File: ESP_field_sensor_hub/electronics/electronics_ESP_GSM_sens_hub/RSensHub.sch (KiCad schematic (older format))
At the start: 42 parts, among them J1 RJ45_Shielded, J2 RJ45_Shielded, J4 Conn_01x04_Female, Q4 IRF540N, U1 MAX48_module, U10 PC817, U11 PC817, U12 PC817, U2 5V5ADCDC, U3 ESP32-WROOM-32U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

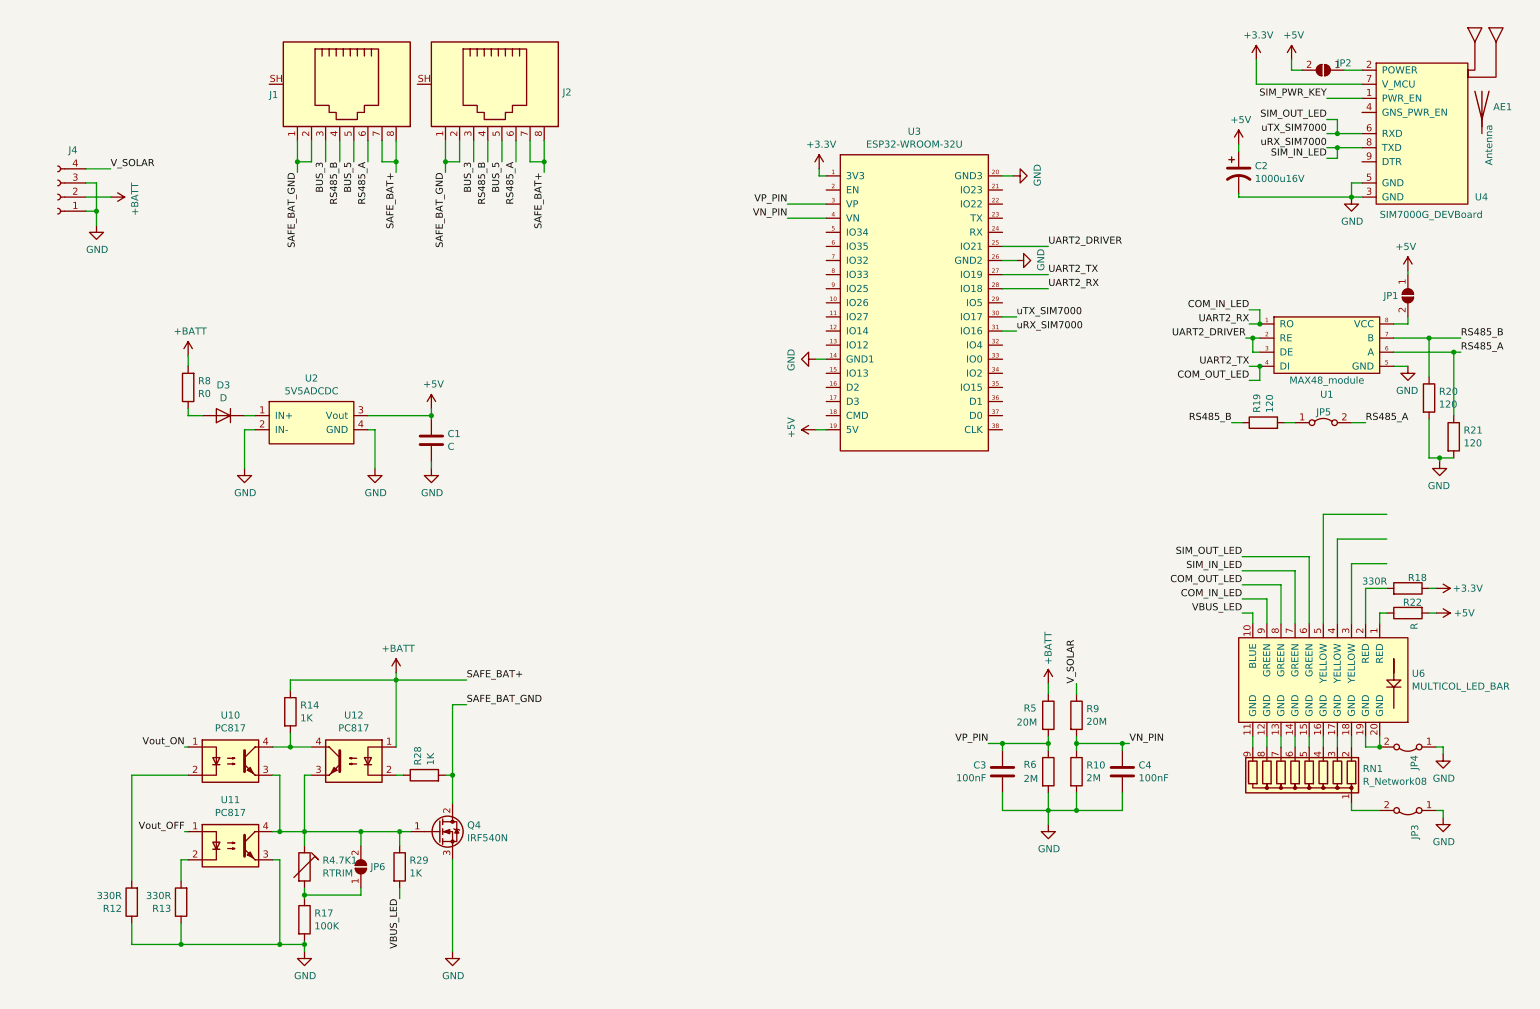
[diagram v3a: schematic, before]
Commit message: worked on sens hub PCB layout, mostly done, needs finishing touches
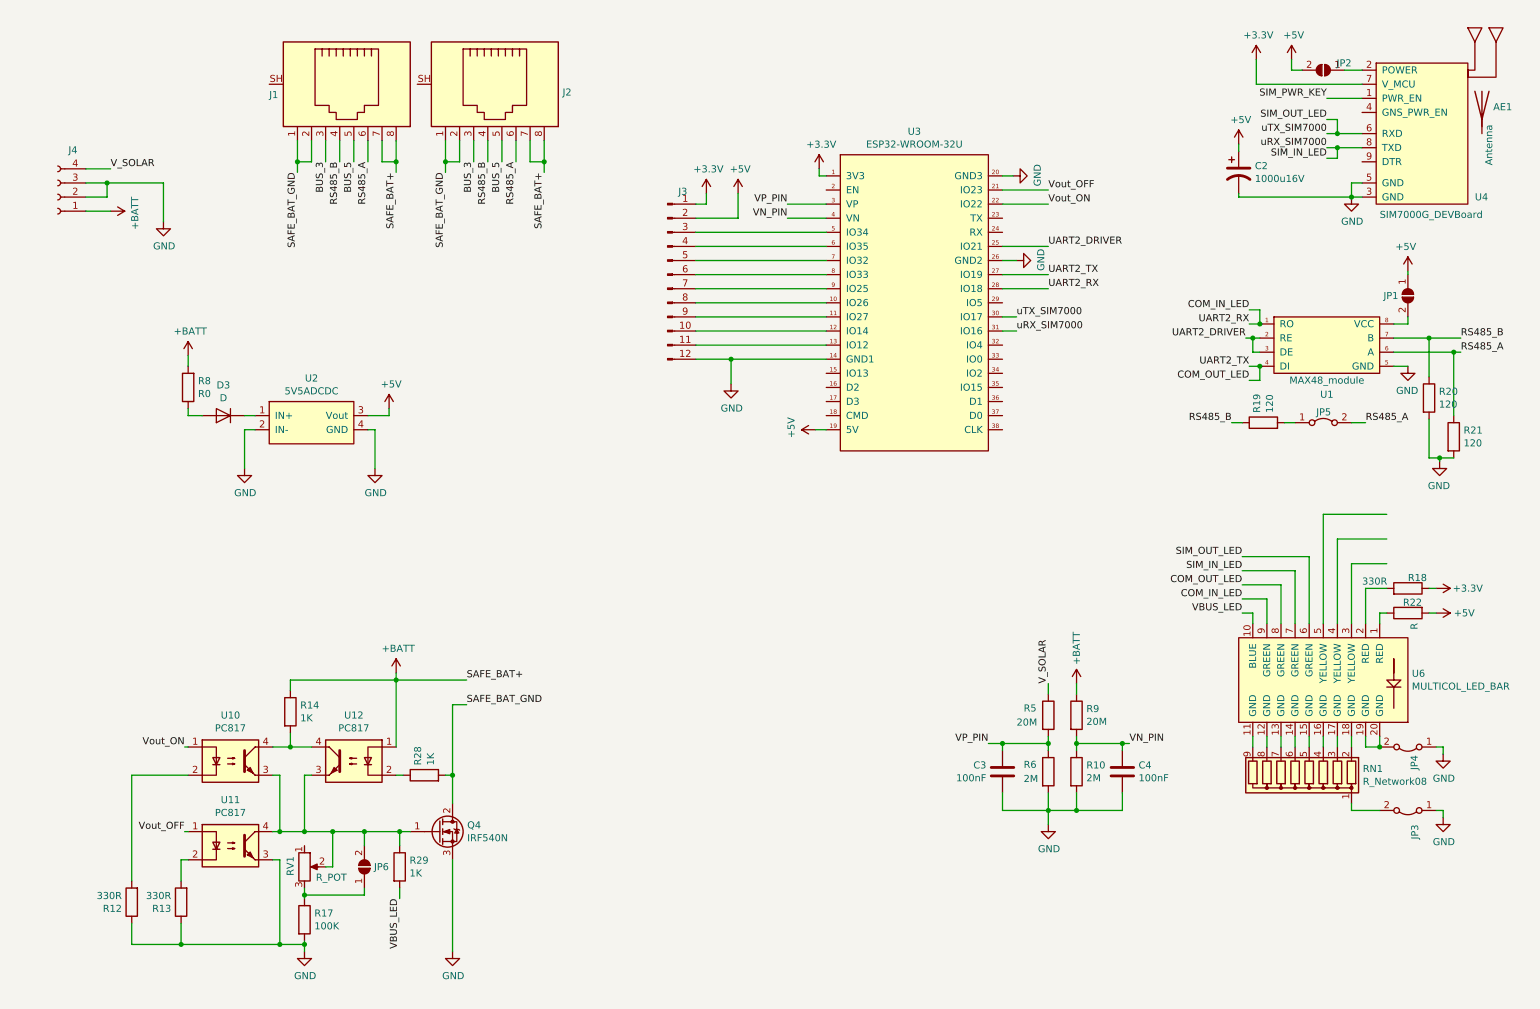
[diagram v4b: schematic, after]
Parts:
- removed C1: C, symbol Device:C
- removed R4.7K1: RTRIM, symbol Device:RTRIM
- added J3: Conn_01x12_Male, myComponents:PinHeader_1x12_P2.54mm_widePads, symbol Connector:Conn_01x12_Male
- added RV1: R_POT, myComponents:Potentiometer_ACP_CA9-V10_Vertical_Hole, symbol Device:R_POT
- D3: footprint (none) -> myComponents:1N41_Diode
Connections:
- net +3V3: now also J3.1 (Pin_1)
- net +5V: now also J3.2 (Pin_2)
- net +BATT: now also J4.1 (Pin_1), R9.1; no longer J4.2 (Pin_2), R5.1
- net GND: now also J4.2 (Pin_2), J3.12 (Pin_12); no longer J4.1 (Pin_1)
- net V_SOLAR: now also R5.1; no longer R9.1
- net Vout_OFF: now also U3.21 (IO23)
- net Vout_ON: now also U3.22 (IO22)
- net at U3.10 (IO26): now also J3.8 (Pin_8)
- net at U3.11 (IO27): now also J3.9 (Pin_9)
- net at U3.12 (IO14): now also J3.10 (Pin_10)
- net at U3.13 (IO12): now also J3.11 (Pin_11)
- net at U3.5 (IO34): now also J3.3 (Pin_3)
- net at U3.6 (IO35): now also J3.4 (Pin_4)
- net at U3.7 (IO32): now also J3.5 (Pin_5)
- net at U3.8 (IO33): now also J3.6 (Pin_6)
- net at U3.9 (IO25): now also J3.7 (Pin_7)
- net at JP6.2 (B), Q4.1 (G), R29.1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: now also RV1.2
- net at JP6.1 (A), R17.1: now also RV1.3
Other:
- moved on the sheet: JP6
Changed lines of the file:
@@
 L power:+BATT #PWR0111
 U 1 1 636D9491
-P 7825 5250
-F 0 "#PWR0111" H 7825 5100 50  0001 C CNN
-F 1 "+BATT" V 7825 5500 50  0000 C CNN
-F 2 "" H 7825 5250 50  0001 C CNN
-F 3 "" H 7825 5250 50  0001 C CNN
-	1    7825 5250
+P 8025 5250
+F 0 "#PWR0111" H 8025 5100 50  0001 C CNN
+F 1 "+BATT" V 8025 5500 50  0000 C CNN
+F 2 "" H 8025 5250 50  0001 C CNN
+F 3 "" H 8025 5250 50  0001 C CNN
+	1    8025 5250
 	1    0    0    -1
 $EndComp
@@
 	2200 3350 2125 3350
 Wire Wire Line
-	3000 3350 3450 3350
-Wire Wire Line
-	3450 3350 3450 3300
+	3150 3350 3150 3300
 $Comp
 L power:+5V #PWR0115
 U 1 1 636A3668
-P 3450 3300
-F 0 "#PWR0115" H 3450 3150 50  0001 C CNN
-F 1 "+5V" H 3465 3473 50  0000 C CNN
-F 2 "" H 3450 3300 50  0001 C CNN
-F 3 "" H 3450 3300 50  0001 C CNN
-	1    3450 3300
-	1    0    0    -1
-$EndComp
-$Comp
-L Device:C C1
-U 1 1 636A4A02
-P 3450 3525
-F 0 "C1" H 3565 3571 50  0000 L CNN
-F 1 "C" H 3565 3480 50  0000 L CNN
-F 2 "" H 3488 3375 50  0001 C CNN
-F 3 "~" H 3450 3525 50  0001 C CNN
-	1    3450 3525
-	1    0    0    -1
-$EndComp
-Wire Wire Line
-	3450 3375 3450 3350
-Connection ~ 3450 3350
-Wire Wire Line
-	3450 3675 3450 3725
-$Comp
-L power:GND #PWR0116
-U 1 1 636A7644
-P 3450 3725
-F 0 "#PWR0116" H 3450 3475 50  0001 C CNN
-F 1 "GND" H 3455 3552 50  0000 C CNN
-F 2 "" H 3450 3725 50  0001 C CNN
-F 3 "" H 3450 3725 50  0001 C CNN
-	1    3450 3725
+P 3150 3300
+F 0 "#PWR0115" H 3150 3150 50  0001 C CNN
+F 1 "+5V" H 3165 3473 50  0000 C CNN
+F 2 "" H 3150 3300 50  0001 C CNN
+F 3 "" H 3150 3300 50  0001 C CNN
+	1    3150 3300
 	1    0    0    -1
 $EndComp
@@
 F 0 "D3" H 1975 3134 50  0000 C CNN
 F 1 "D" H 1975 3225 50  0000 C CNN
-F 2 "" H 1975 3350 50  0001 C CNN
+F 2 "myComponents:1N41_Diode" H 1975 3350 50  0001 C CNN
 F 3 "~" H 1975 3350 50  0001 C CNN
 	1    1975 3350
@@
 Wire Wire Line
 	8025 5325 8025 5250
-Text Label 8025 5250 1    50   ~ 0
+Text Label 7825 5250 1    50   ~ 0
 V_SOLAR
 Wire Wire Line
@@
 	-1   0    0    1
 $EndComp
-$Comp
-L power:+BATT #PWR0130
-U 1 1 63985720
-P 1175 1800
-F 0 "#PWR0130" H 1175 1650 50  0001 C CNN
-F 1 "+BATT" H 1190 1973 50  0000 C CNN
-F 2 "" H 1175 1800 50  0001 C CNN
-F 3 "" H 1175 1800 50  0001 C CNN
-	1    1175 1800
-	0    1    1    0
-$EndComp
-$Comp
-L power:GND #PWR0131
-U 1 1 6398F99C
-P 1075 2000
-F 0 "#PWR0131" H 1075 1750 50  0001 C CNN
-F 1 "GND" H 1080 1827 50  0000 C CNN
-F 2 "" H 1075 2000 50  0001 C CNN
-F 3 "" H 1075 2000 50  0001 C CNN
-	1    1075 2000
-	1    0    0    -1
-$EndComp
-Wire Wire Line
-	1000 1900 1075 1900
-Wire Wire Line
-	1075 1900 1075 2000
-Wire Wire Line
-	1000 1700 1075 1700
-Wire Wire Line
-	1075 1700 1075 1900
-Connection ~ 1075 1900
 Text Label 1175 1600 0    50   ~ 0
 V_SOLAR
@@
 L power:GND #PWR0136
 U 1 1 63D67849
-P 6175 2950
-F 0 "#PWR0136" H 6175 2700 50  0001 C CNN
-F 1 "GND" H 6180 2777 50  0000 C CNN
-F 2 "" H 6175 2950 50  0001 C CNN
-F 3 "" H 6175 2950 50  0001 C CNN
-	1    6175 2950
-	0    1    1    0
-$EndComp
-Wire Wire Line
-	6175 2950 6250 2950
+P 5575 3125
+F 0 "#PWR0136" H 5575 2875 50  0001 C CNN
+F 1 "GND" H 5580 2952 50  0000 C CNN
+F 2 "" H 5575 3125 50  0001 C CNN
+F 3 "" H 5575 3125 50  0001 C CNN
+	1    5575 3125
+	1    0    0    -1
+$EndComp
 $Comp
 L power:+5V #PWR0137
@@
 Text Label 4250 1625 3    50   ~ 0
 SAFE_BAT+
-Wire Wire Line
-	1000 1800 1175 1800
 $Comp
 L Isolator:PC817 U12
@@
 Wire Wire Line
 	3250 5900 3200 5900
-$Comp
-L Device:RTRIM R4.7K1
-U 1 1 6425482E
-P 2550 6550
-F 0 "R4.7K1" H 2678 6596 50  0000 L CNN
-F 1 "RTRIM" H 2678 6505 50  0000 L CNN
-F 2 "" V 2480 6550 50  0001 C CNN
-F 3 "~" H 2550 6550 50  0001 C CNN
-	1    2550 6550
-	1    0    0    -1
-$EndComp
-Wire Wire Line
-	2550 6400 2550 6300
-Wire Wire Line
-	2550 6775 2550 6750
 Wire Wire Line
 	2550 7150 2550 7100
@@
 L Jumper:SolderJumper_2_Open JP6
 U 1 1 644467F2
-P 2950 6550
-F 0 "JP6" V 2950 6618 50  0000 L CNN
-F 1 "SolderJumper_2_Open" H 2950 6664 50  0001 C CNN
-F 2 "Jumper:SolderJumper-2_P1.3mm_Open_RoundedPad1.0x1.5mm" H 2950 6550 50  0001 C CNN
-F 3 "~" H 2950 6550 50  0001 C CNN
-	1    2950 6550
+P 2975 6550
+F 0 "JP6" V 2975 6618 50  0000 L CNN
+F 1 "SolderJumper_2_Open" H 2975 6664 50  0001 C CNN
+F 2 "Jumper:SolderJumper-2_P1.3mm_Open_RoundedPad1.0x1.5mm" H 2975 6550 50  0001 C CNN
+F 3 "~" H 2975 6550 50  0001 C CNN
+	1    2975 6550
 	0    1    -1   0
 $EndComp
 Wire Wire Line
-	2550 6300 2950 6300
-Wire Wire Line
-	2950 6750 2550 6750
-Wire Wire Line
-	2950 6700 2950 6750
-Connection ~ 2550 6750
-Wire Wire Line
-	2550 6750 2550 6700
-Wire Wire Line
-	2950 6400 2950 6300
-Connection ~ 2950 6300
-Wire Wire Line
-	2950 6300 3225 6300
+	2550 6300 2750 6300
 Connection ~ 3225 6300
 Wire Wire Line
@@
 Wire Wire Line
 	1700 5700 1725 5700
+$Comp
+L Device:R_POT RV1
+U 1 1 63DF64FA
+P 2550 6550
+F 0 "RV1" V 2450 6625 50  0000 R CNN
+F 1 "R_POT" H 2850 6475 50  0000 R CNN
+F 2 "myComponents:Potentiometer_ACP_CA9-V10_Vertical_Hole" H 2550 6550 50  0001 C CNN
+F 3 "~" H 2550 6550 50  0001 C CNN
+	1    2550 6550
+	1    0    0    -1
+$EndComp
+Wire Wire Line
+	2700 6550 2750 6550
+Wire Wire Line
+	2750 6550 2750 6300
+Connection ~ 2750 6300
+Wire Wire Line
+	2750 6300 2975 6300
+Wire Wire Line
+	2550 6700 2550 6750
+Wire Wire Line
+	2975 6400 2975 6300
+Connection ~ 2975 6300
+Wire Wire Line
+	2975 6300 3225 6300
+Wire Wire Line
+	2975 6700 2975 6750
+Wire Wire Line
+	2975 6750 2550 6750
+Connection ~ 2550 6750
+Wire Wire Line
+	2550 6750 2550 6775
+Text Label 7825 1850 0    50   ~ 0
+Vout_ON
+Text Label 7825 1750 0    50   ~ 0
+Vout_OFF
+Wire Wire Line
+	7500 1850 7825 1850
+Wire Wire Line
+	7825 1750 7500 1750
+Wire Wire Line
+	5325 2050 6250 2050
+Wire Wire Line
+	5325 2150 6250 2150
+Wire Wire Line
+	5325 2250 6250 2250
+Wire Wire Line
+	5325 2350 6250 2350
+Wire Wire Line
+	6250 2450 5325 2450
+Wire Wire Line
+	5325 2550 6250 2550
+Wire Wire Line
+	6250 2650 5325 2650
+Wire Wire Line
+	6250 2750 5325 2750
+Wire Wire Line
+	6250 2850 5325 2850
+$Comp
+L power:+3.3V #PWR0103
+U 1 1 63EBB881
+P 5400 1775
+F 0 "#PWR0103" H 5400 1625 50  0001 C CNN
+F 1 "+3.3V" H 5415 1948 50  0000 C CNN
+F 2 "" H 5400 1775 50  0001 C CNN
+F 3 "" H 5400 1775 50  0001 C CNN
+	1    5400 1775
+	1    0    0    -1
+$EndComp
+Wire Wire Line
+	5325 1850 5400 1850
+Wire Wire Line
+	5400 1850 5400 1775
+$Comp
+L power:+5V #PWR0104
+U 1 1 63ECC4A0
+P 5625 1775
+F 0 "#PWR0104" H 5625 1625 50  0001 C CNN
+F 1 "+5V" H 5640 1948 50  0000 C CNN
+F 2 "" H 5625 1775 50  0001 C CNN
+F 3 "" H 5625 1775 50  0001 C CNN
+	1    5625 1775
+	1    0    0    -1
+$EndComp
+Wire Wire Line
+	5325 1950 5625 1950
+Wire Wire Line
+	5625 1950 5625 1775
+$Comp
+L Connector:Conn_01x12_Male J3
+U 1 1 63F520BD
+P 5125 2350
+F 0 "J3" H 5233 2939 50  0000 C CNN
+F 1 "Conn_01x12_Male" H 5233 2940 50  0001 C CNN
+F 2 "myComponents:PinHeader_1x12_P2.54mm_widePads" H 5125 2350 50  0001 C CNN
+F 3 "~" H 5125 2350 50  0001 C CNN
+	1    5125 2350
+	1    0    0    -1
+$EndComp
+Wire Wire Line
+	5325 2950 5575 2950
+Wire Wire Line
+	5575 3125 5575 2950
+Connection ~ 5575 2950
+Wire Wire Line
+	5575 2950 6250 2950
+$Comp
+L power:GND #PWR0131
+U 1 1 6398F99C
+P 1550 1975
+F 0 "#PWR0131" H 1550 1725 50  0001 C CNN
+F 1 "GND" H 1555 1802 50  0000 C CNN
+F 2 "" H 1550 1975 50  0001 C CNN
+F 3 "" H 1550 1975 50  0001 C CNN
+	1    1550 1975
+	1    0    0    -1
+$EndComp
+$Comp
+L power:+BATT #PWR0130
+U 1 1 63985720
+P 1175 1900
+F 0 "#PWR0130" H 1175 1750 50  0001 C CNN
+F 1 "+BATT" H 1190 2073 50  0000 C CNN
+F 2 "" H 1175 1900 50  0001 C CNN
+F 3 "" H 1175 1900 50  0001 C CNN
+	1    1175 1900
+	0    1    1    0
+$EndComp
+Wire Wire Line
+	1175 1900 1000 1900
+Wire Wire Line
+	1000 1700 1150 1700
+Wire Wire Line
+	1550 1700 1550 1975
+Wire Wire Line
+	1000 1800 1150 1800
+Wire Wire Line
+	1150 1800 1150 1700
+Connection ~ 1150 1700
+Wire Wire Line
+	1150 1700 1550 1700
+Wire Wire Line
+	3000 3350 3150 3350
 $EndSCHEMATC

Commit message: started working on GNSS time and NTP functionality, ESP32 timekeeping works, just need to update it from modem. need to parse the GNSS status for string. Played around with chatGPT, and got a fairly good solution for converting datetimeString to unix time. @TODO: the SIM7000 class makes little sense, needs a refactoring. I have functions for geting CSQ and GNSS data from modem in a totally different class.
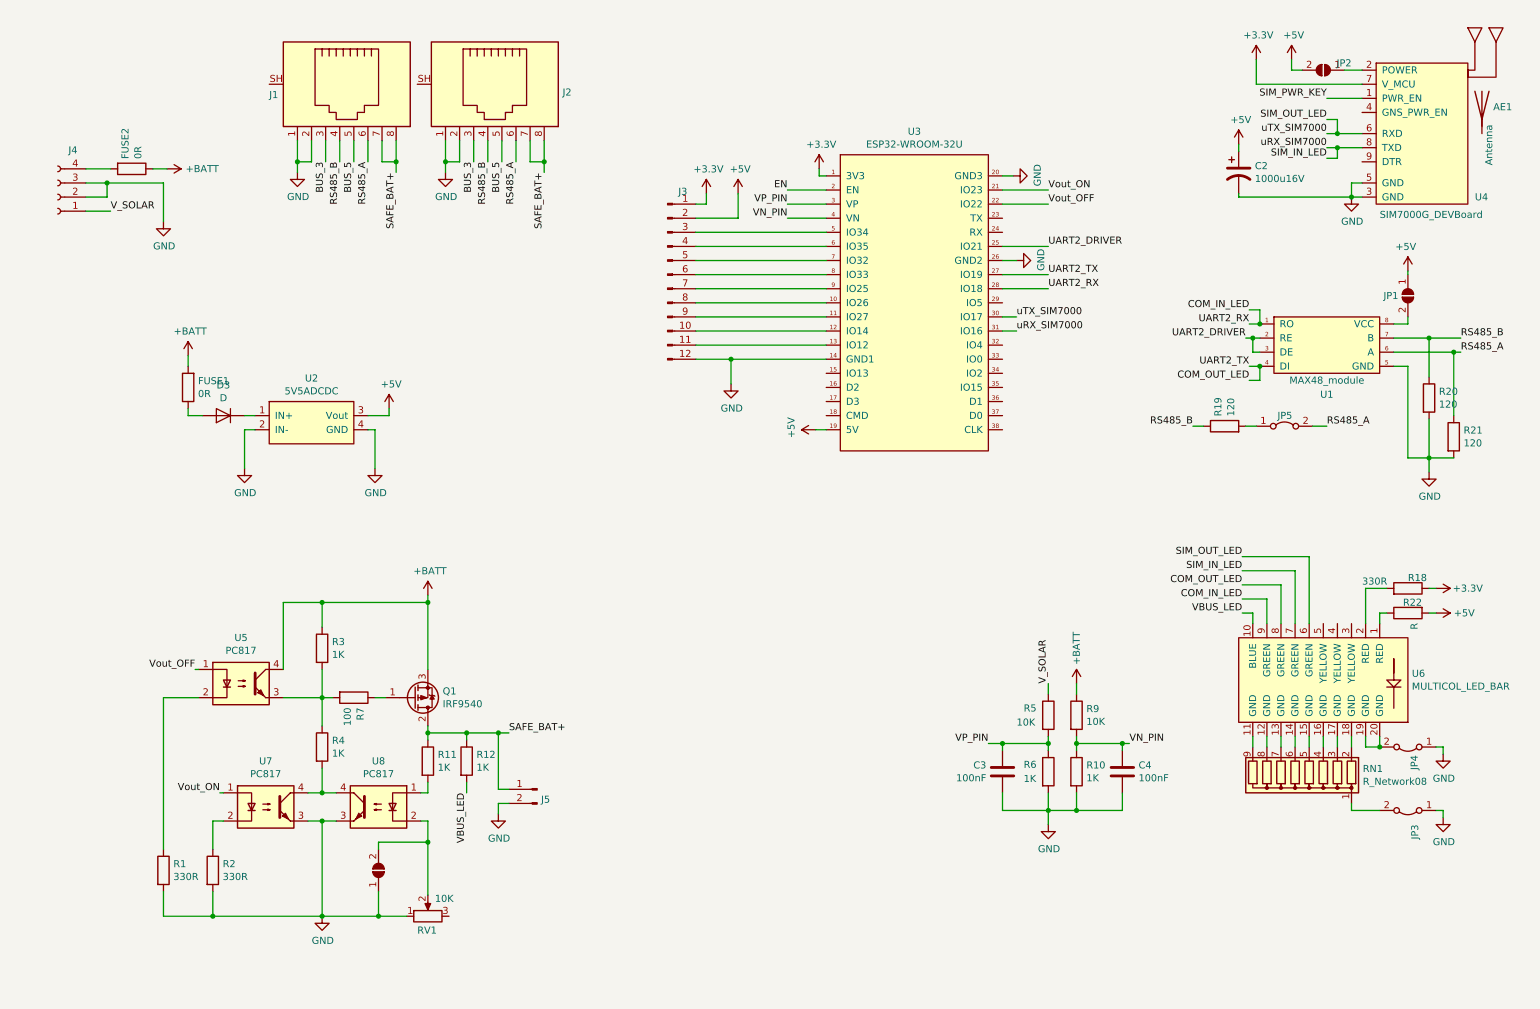
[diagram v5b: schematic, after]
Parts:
- removed Q4: IRF540N, myComponents:TO-220-3_Horizontal_TabDown_bothSides, symbol Transistor_FET:IRF540N
- removed R13: 330R, myComponents:resistor0.25,9mm, symbol Device:R
- removed R14, R28, R29: 1K, myComponents:resistor0.25,9mm, symbol Device:R
- removed R17: 100K, myComponents:resistor0.25,9mm, symbol Device:R
- removed U10, U11, U12: PC817, myComponents:optoCouplerDIP4, symbol Isolator:PC817
- added FUSE2: 0R, myComponents:resistor0.25,9mm, symbol Device:R
- added J5: Conn_01x02_Male, myComponents:TerminalBlockRemovablex2, symbol Connector:Conn_01x02_Male
- added Q1: IRF9540, myComponents:TO-220-3_Horizontal_TabDown_bothSides, symbol Device:Q_PMOS_GDS
- added R1, R2: 330R, myComponents:resistor0.25,9mm, symbol Device:R
- added R11, R3, R4: 1K, myComponents:resistor0.25,9mm, symbol Device:R
- added R7: 100, myComponents:resistor0.25,9mm, symbol Device:R
- added U5, U7, U8: PC817, myComponents:optoCouplerDIP4, symbol Isolator:PC817
- FUSE1: renamed from R8; value R0 -> 0R
- R10, R6: value 2M -> 1K
- R12: value 330R -> 1K
- R5, R9: value 20M -> 10K
- RV1: value R_POT -> 10K
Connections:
- net SAFE_BAT_GND is gone; now on net GND: J1.1, J1.2, J2.1, J2.2
- net +BATT: now also FUSE2.1, Q1.3 (S), R3.1, U5.4; no longer J1.7, J1.8, J2.7, J2.8, J4.1 (Pin_1)
- net GND: now also JP6.1 (A), RV1.1, J5.2 (Pin_2), R1.2, R2.2, U7.3, U8.3; no longer R12.1
- net VBUS_LED: now also R12.2
- net V_SOLAR: now also J4.1 (Pin_1); no longer J4.4 (Pin_4)
- net Vout_OFF: now also U3.22 (IO22), U5.1; no longer U3.21 (IO23)
- net Vout_ON: now also U3.21 (IO23), U7.1; no longer U3.22 (IO22)
- net EN: now reaches U3.2 (EN)
- net at JP6.2 (B), RV1.2: now also U8.2
- net at RV1.3: no longer JP6.1 (A)
- new net: FUSE2.2, J4.4 (Pin_4)
- new net: R11.2, U8.1
- new net: R4.2, U7.4, U8.4
- new net: R1.1, U5.2
- new net: R3.2, R4.1, R7.2, U5.3
- new net: R2.1, U7.2
- new net: Q1.1 (G), R7.1
- new net SAFE_BAT+: J1.7, J1.8, J2.7, J2.8, J5.1 (Pin_1), Q1.2 (D), R11.1, R12.1
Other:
- moved on the sheet: JP5, R19
